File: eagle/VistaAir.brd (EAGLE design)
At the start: 97.3 x 51.9 mm, 11 parts, among them IC1 MCP170312MB, J1 POWER_JACK

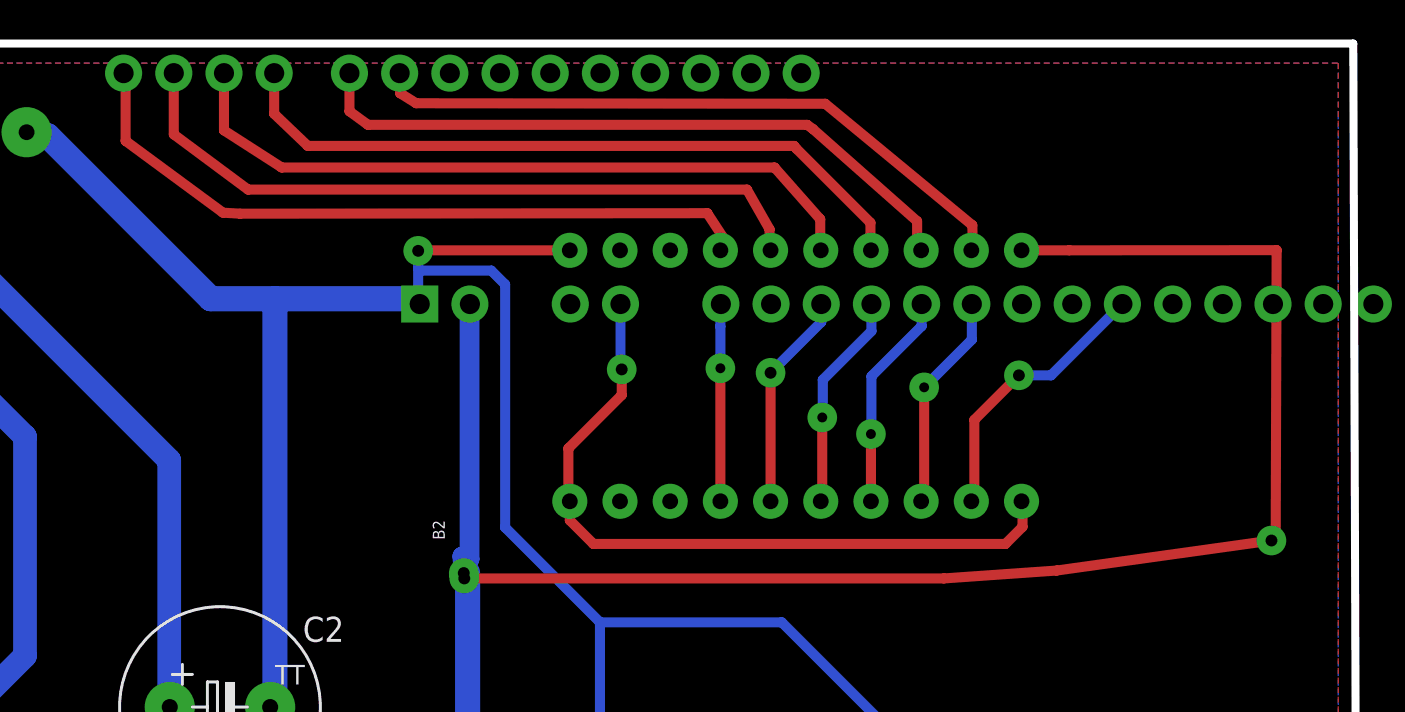
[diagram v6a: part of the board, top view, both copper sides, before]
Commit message: using one way logic translator since motor driver PWM inputs are open drain - and sets up ultra-high-frequency push pull with bi-directional logic shifter
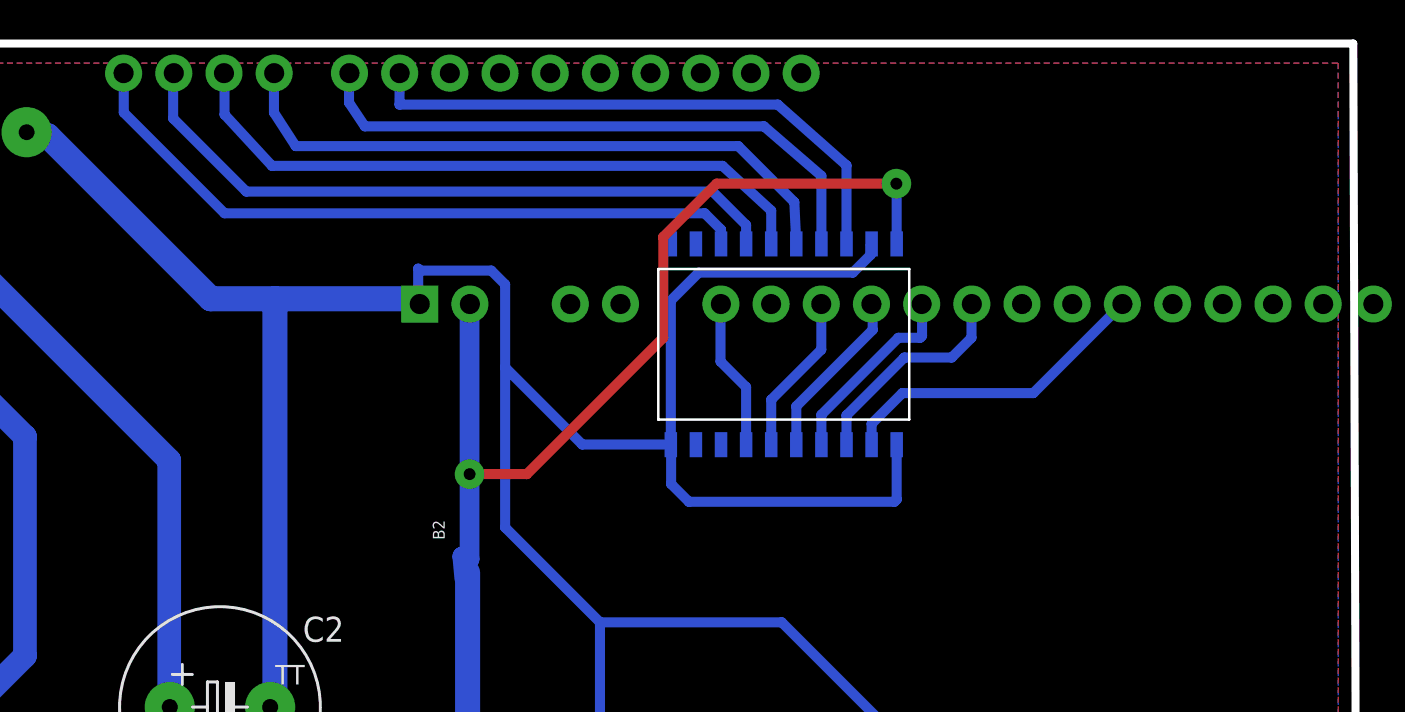
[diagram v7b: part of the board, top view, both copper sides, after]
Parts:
- removed U$3: 8_CHANNEL_LOGIC_CONVERTER, kevins_parts:8_CHANNEL_LOGIC_CONVERTER
- added U$1: SN74AHCT541_SOIC-20, kevins_parts:SN74AHCT541
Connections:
- removed net 3V3: B2.5, U$3.OE, U$3.VA
- net BOARD_GND: now also U$1.GND, U$1.OE1, U$1.OE2; no longer U$3.GND
- net CCL1_3V3: now also U$1.A2; no longer U$3.A2
- net CCL1_5V: now also U$1.Y2; no longer U$3.B2
- net CCL2_3V3: now also U$1.A1; no longer U$3.A1
- net CCL2_5V: now also U$1.Y1; no longer U$3.B1
- net CLW1_3V3: now also U$1.A3; no longer U$3.A3
- net CLW1_5V: now also U$1.Y3; no longer U$3.B3
- net CLW2_3V3: now also U$1.A6; no longer U$3.A6
- net CLW2_5V: now also U$1.Y6; no longer U$3.B6
- net PWM1_3V3: now also U$1.A5; no longer U$3.A5
- net PWM1_5V: now also U$1.Y5; no longer U$3.B5
- net PWM2_3V3: now also U$1.A4; no longer U$3.A4
- net PWM2_5V: now also U$1.Y4; no longer U$3.B4
- net V5IN: now also U$1.VCC; no longer U$3.VB
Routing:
- net 3V3: track 37.2 -> 0.00 mm, vias 1 -> 0
- net BOARD_GND: track 183.3 -> 220.2 mm, vias 1 -> 0
- net V5IN: track 143.4 -> 107.9 mm, vias 3 -> 2
- net CCL2_5V: track 33.6 -> 29.4 mm
- net CCL1_5V: track 34.3 -> 30.4 mm
- net CLW1_5V: track 35.9 -> 32.5 mm
- net PWM2_5V: track 36.4 -> 33.5 mm
- net PWM1_3V3: track 11.0 -> 8.17 mm, vias 1 -> 0
- net CLW2_3V3: track 9.98 -> 7.66 mm, vias 1 -> 0
- net PWM2_3V3: track 11.0 -> 8.74 mm, vias 1 -> 0
- net CCL2_3V3: track 14.1 -> 16.3 mm, vias 1 -> 0
- net PWM1_5V: track 36.4 -> 34.5 mm
- net CLW1_3V3: track 11.0 -> 9.88 mm, vias 1 -> 0
- net CLW2_5V: track 36.3 -> 35.4 mm
- net CCL1_3V3: track 11.0 -> 11.2 mm, vias 1 -> 0
